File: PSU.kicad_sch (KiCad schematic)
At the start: 55 parts, among them J1 ~12VAC_A, J10 GND, J11 -12V, J12 +5V, J2 ~12VAC_A, J3 ~12VAC_B, J4 ~12VAC_B, J9 +12V, U1 LM317_TO-220, U2 LM317_TO-220, U3 LM337_TO220

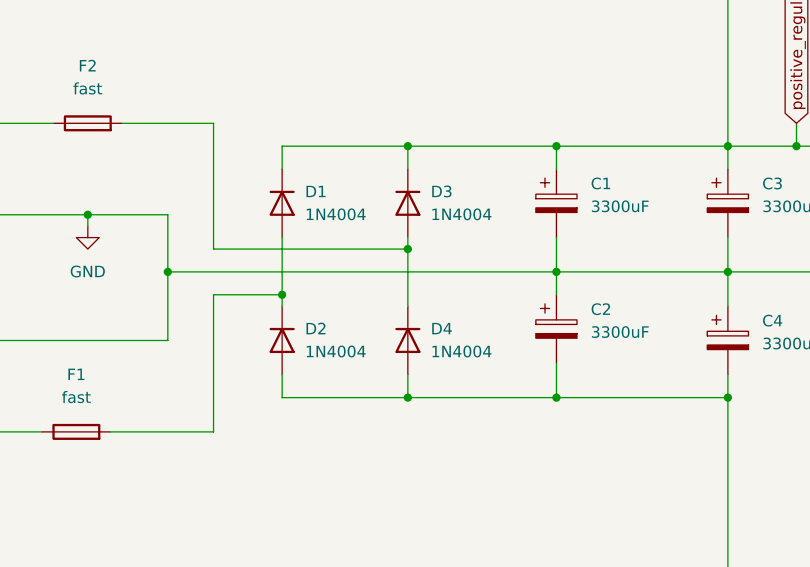
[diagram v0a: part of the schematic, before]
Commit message: Swap rectifier diodes for larger ones. Change input terminal text to be more legible.
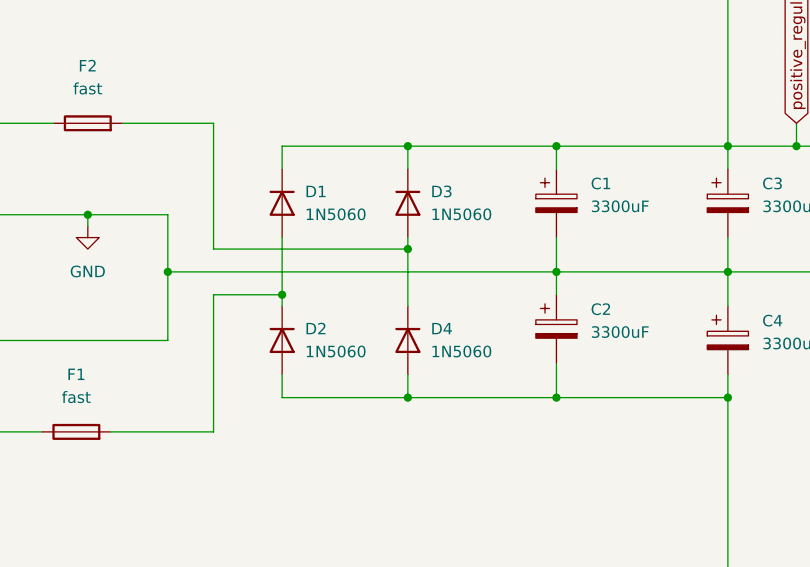
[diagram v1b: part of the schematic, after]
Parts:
- D1, D2, D3, D4: value 1N4004 -> 1N5060
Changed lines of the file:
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@@
       (effects (font (size 1.27 1.27)) (justify left))
     )
-    (property "Value" "1N4004" (id 1) (at 87.63 104.1399 90)
+    (property "Value" "1N5060" (id 1) (at 87.63 104.1399 90)
       (effects (font (size 1.27 1.27)) (justify left))
     )
@@
       (effects (font (size 1.27 1.27)) (justify left))
     )
-    (property "Value" "1N4004" (id 1) (at 101.6 104.1399 90)
+    (property "Value" "1N5060" (id 1) (at 101.6 104.1399 90)
       (effects (font (size 1.27 1.27)) (justify left))
     )
@@
       (effects (font (size 1.27 1.27)) (justify left))
     )
-    (property "Value" "1N4004" (id 1) (at 101.6 88.8999 90)
+    (property "Value" "1N5060" (id 1) (at 101.6 88.8999 90)
       (effects (font (size 1.27 1.27)) (justify left))
     )
@@
       (effects (font (size 1.27 1.27)) (justify left))
     )
-    (property "Value" "1N4004" (id 1) (at 87.63 88.8999 90)
+    (property "Value" "1N5060" (id 1) (at 87.63 88.8999 90)
       (effects (font (size 1.27 1.27)) (justify left))
     )
@@
     )
     (path "/f34b4507-f5d7-4b15-9ede-8d76d9cea360"
-      (reference "D1") (unit 1) (value "1N4004") (footprint "Diode_THT:D_DO-41_SOD81_P10.16mm_Horizontal")
+      (reference "D1") (unit 1) (value "1N5060") (footprint "Diode_THT:D_DO-41_SOD81_P10.16mm_Horizontal")
     )
     (path "/31c7e7d4-2566-4ceb-b304-6dfc36679056"
-      (reference "D2") (unit 1) (value "1N4004") (footprint "Diode_THT:D_DO-41_SOD81_P10.16mm_Horizontal")
+      (reference "D2") (unit 1) (value "1N5060") (footprint "Diode_THT:D_DO-41_SOD81_P10.16mm_Horizontal")
     )
     (path "/9705ebf1-c2ec-44a4-8cff-df85e62870ac"
-      (reference "D3") (unit 1) (value "1N4004") (footprint "Diode_THT:D_DO-41_SOD81_P10.16mm_Horizontal")
+      (reference "D3") (unit 1) (value "1N5060") (footprint "Diode_THT:D_DO-41_SOD81_P10.16mm_Horizontal")
     )
     (path "/5937859a-61e8-45ba-9ebc-1202e95598fd"
-      (reference "D4") (unit 1) (value "1N4004") (footprint "Diode_THT:D_DO-41_SOD81_P10.16mm_Horizontal")
+      (reference "D4") (unit 1) (value "1N5060") (footprint "Diode_THT:D_DO-41_SOD81_P10.16mm_Horizontal")
     )
     (path "/c155e713-676d-49b4-a2d9-40174c28c34c"

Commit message: Edit input label text
Change input labels for improved legibility
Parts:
- D1, D2, D3, D4: footprint Diode_THT:D_DO-41_SOD81_P10.16mm_Horizontal -> Diode_THT:D_DO-15_P10.16mm_Horizontal
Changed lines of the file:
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@@
   (title_block
     (title "Eurorack PSU")
-    (rev "0.1.0")
+    (rev "0.2.0")
     (company "Butch Warns")
   )
@@
       (effects (font (size 1.27 1.27)) (justify left))
     )
-    (property "Footprint" "Diode_THT:D_DO-41_SOD81_P10.16mm_Horizontal" (id 2) (at 80.645 102.87 0)
+    (property "Footprint" "Diode_THT:D_DO-15_P10.16mm_Horizontal" (id 2) (at 80.645 102.87 0)
       (effects (font (size 1.27 1.27)) hide)
     )
@@
       (effects (font (size 1.27 1.27)) (justify left))
     )
-    (property "Footprint" "Diode_THT:D_DO-41_SOD81_P10.16mm_Horizontal" (id 2) (at 94.615 102.87 0)
+    (property "Footprint" "Diode_THT:D_DO-15_P10.16mm_Horizontal" (id 2) (at 94.615 102.87 0)
       (effects (font (size 1.27 1.27)) hide)
     )
@@
       (effects (font (size 1.27 1.27)) (justify left))
     )
-    (property "Footprint" "Diode_THT:D_DO-41_SOD81_P10.16mm_Horizontal" (id 2) (at 94.615 87.63 0)
+    (property "Footprint" "Diode_THT:D_DO-15_P10.16mm_Horizontal" (id 2) (at 94.615 87.63 0)
       (effects (font (size 1.27 1.27)) hide)
     )
@@
       (effects (font (size 1.27 1.27)) (justify left))
     )
-    (property "Footprint" "Diode_THT:D_DO-41_SOD81_P10.16mm_Horizontal" (id 2) (at 80.645 87.63 0)
+    (property "Footprint" "Diode_THT:D_DO-15_P10.16mm_Horizontal" (id 2) (at 80.645 87.63 0)
       (effects (font (size 1.27 1.27)) hide)
     )
@@
     )
     (path "/f34b4507-f5d7-4b15-9ede-8d76d9cea360"
-      (reference "D1") (unit 1) (value "1N5060") (footprint "Diode_THT:D_DO-41_SOD81_P10.16mm_Horizontal")
+      (reference "D1") (unit 1) (value "1N5060") (footprint "Diode_THT:D_DO-15_P10.16mm_Horizontal")
     )
     (path "/31c7e7d4-2566-4ceb-b304-6dfc36679056"
-      (reference "D2") (unit 1) (value "1N5060") (footprint "Diode_THT:D_DO-41_SOD81_P10.16mm_Horizontal")
+      (reference "D2") (unit 1) (value "1N5060") (footprint "Diode_THT:D_DO-15_P10.16mm_Horizontal")
     )
     (path "/9705ebf1-c2ec-44a4-8cff-df85e62870ac"
-      (reference "D3") (unit 1) (value "1N5060") (footprint "Diode_THT:D_DO-41_SOD81_P10.16mm_Horizontal")
+      (reference "D3") (unit 1) (value "1N5060") (footprint "Diode_THT:D_DO-15_P10.16mm_Horizontal")
     )
     (path "/5937859a-61e8-45ba-9ebc-1202e95598fd"
-      (reference "D4") (unit 1) (value "1N5060") (footprint "Diode_THT:D_DO-41_SOD81_P10.16mm_Horizontal")
+      (reference "D4") (unit 1) (value "1N5060") (footprint "Diode_THT:D_DO-15_P10.16mm_Horizontal")
     )
     (path "/c155e713-676d-49b4-a2d9-40174c28c34c"

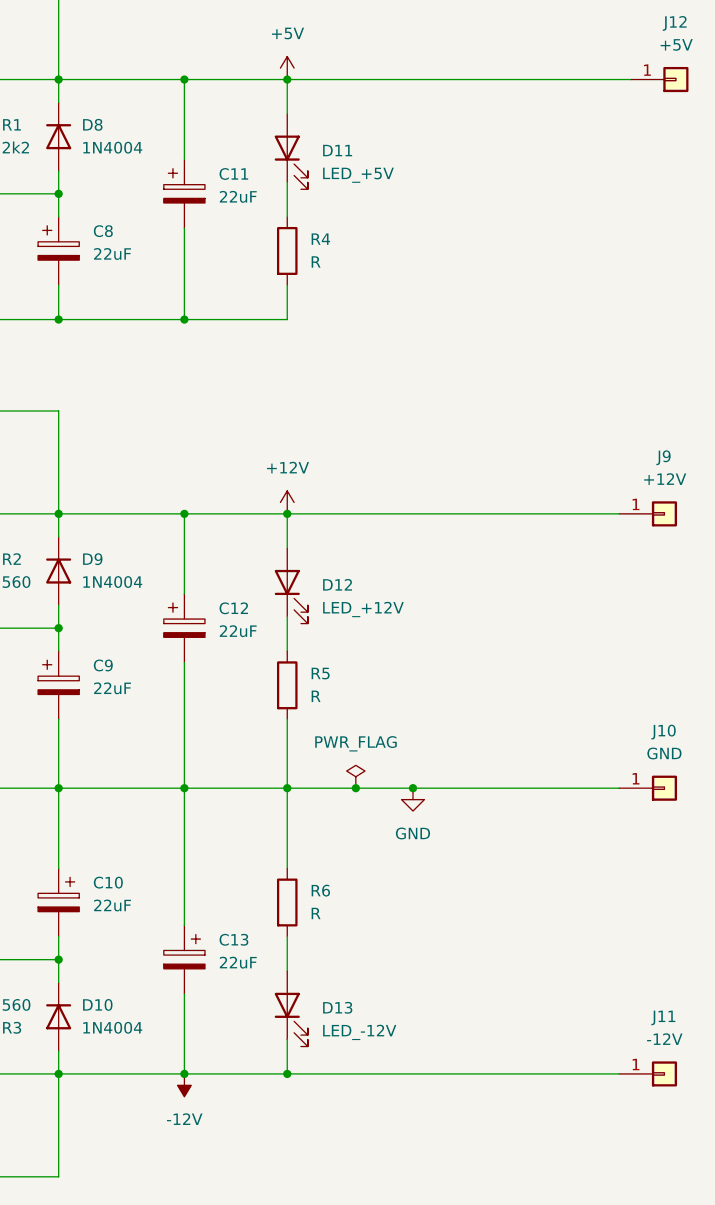
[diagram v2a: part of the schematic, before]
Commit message: Do some small touches before making repo public
Add v010 Gerber files. Add interactive HTML BOM. Set values for LED
current limiting resistors.
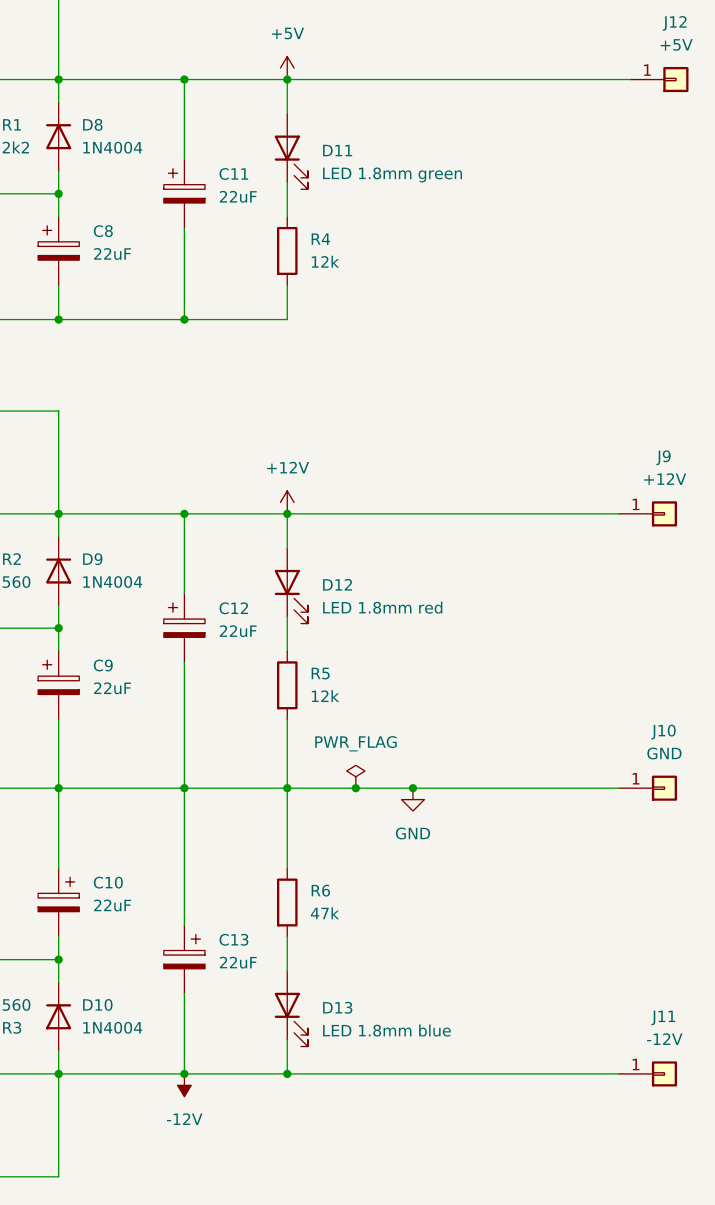
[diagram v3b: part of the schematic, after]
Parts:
- D11: value LED_+5V -> LED 1.8mm green
- D12: value LED_+12V -> LED 1.8mm red
- D13: value LED_-12V -> LED 1.8mm blue
- R4, R5: value R -> 12k
- R6: value R -> 47k
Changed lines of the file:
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@@
       (effects (font (size 1.27 1.27)) (justify right))
     )
-    (property "Value" "LED_-12V" (id 1) (at 222.25 138.7474 90)
+    (property "Value" "LED 1.8mm blue" (id 1) (at 222.25 138.7474 90)
       (effects (font (size 1.27 1.27)) (justify right))
     )
@@
       (effects (font (size 1.27 1.27)) (justify right))
     )
-    (property "Value" "LED_+5V" (id 1) (at 222.25 43.4974 90)
+    (property "Value" "LED 1.8mm green" (id 1) (at 222.25 43.4974 90)
       (effects (font (size 1.27 1.27)) (justify right))
     )
@@
       (effects (font (size 1.27 1.27)) (justify left))
     )
-    (property "Value" "R" (id 1) (at 220.98 101.5999 0)
+    (property "Value" "12k" (id 1) (at 220.98 101.5999 0)
       (effects (font (size 1.27 1.27)) (justify left))
     )
@@
       (effects (font (size 1.27 1.27)) (justify right))
     )
-    (property "Value" "LED_+12V" (id 1) (at 222.25 91.7574 90)
+    (property "Value" "LED 1.8mm red" (id 1) (at 222.25 91.7574 90)
       (effects (font (size 1.27 1.27)) (justify right))
     )
@@
       (effects (font (size 1.27 1.27)) (justify left))
     )
-    (property "Value" "R" (id 1) (at 220.98 53.3399 0)
+    (property "Value" "12k" (id 1) (at 220.98 53.3399 0)
       (effects (font (size 1.27 1.27)) (justify left))
     )
@@
       (effects (font (size 1.27 1.27)) (justify left))
     )
-    (property "Value" "R" (id 1) (at 220.98 125.7299 0)
+    (property "Value" "47k" (id 1) (at 220.98 125.7299 0)
       (effects (font (size 1.27 1.27)) (justify left))
     )
@@
     )
     (path "/1a920980-a2b1-45eb-ac3e-2649db811b22"
-      (reference "D11") (unit 1) (value "LED_+5V") (footprint "LED_THT:LED_D3.0mm")
+      (reference "D11") (unit 1) (value "LED 1.8mm green") (footprint "LED_THT:LED_D3.0mm")
     )
     (path "/7a29d124-ffbb-483f-8475-3c260e713647"
-      (reference "D12") (unit 1) (value "LED_+12V") (footprint "LED_THT:LED_D3.0mm")
+      (reference "D12") (unit 1) (value "LED 1.8mm red") (footprint "LED_THT:LED_D3.0mm")
     )
     (path "/05521341-4993-41a8-8e86-233c58d1545c"
-      (reference "D13") (unit 1) (value "LED_-12V") (footprint "LED_THT:LED_D3.0mm")
+      (reference "D13") (unit 1) (value "LED 1.8mm blue") (footprint "LED_THT:LED_D3.0mm")
     )
     (path "/e7f7fe4f-ebfb-471a-976d-2ea6e6769e03"
@@
     )
     (path "/8bf15c7b-f15f-4a8b-a9a2-ac115433038f"
-      (reference "R4") (unit 1) (value "R") (footprint "Resistor_THT:R_Axial_DIN0207_L6.3mm_D2.5mm_P7.62mm_Horizontal")
+      (reference "R4") (unit 1) (value "12k") (footprint "Resistor_THT:R_Axial_DIN0207_L6.3mm_D2.5mm_P7.62mm_Horizontal")
     )
     (path "/4d8cb080-1bed-4fdd-a077-e915dc4fb9eb"
-      (reference "R5") (unit 1) (value "R") (footprint "Resistor_THT:R_Axial_DIN0207_L6.3mm_D2.5mm_P7.62mm_Horizontal")
+      (reference "R5") (unit 1) (value "12k") (footprint "Resistor_THT:R_Axial_DIN0207_L6.3mm_D2.5mm_P7.62mm_Horizontal")
     )
     (path "/eae44fa8-75b9-45b0-b4a0-25dcf086bf08"
-      (reference "R6") (unit 1) (value "R") (footprint "Resistor_THT:R_Axial_DIN0207_L6.3mm_D2.5mm_P7.62mm_Horizontal")
+      (reference "R6") (unit 1) (value "47k") (footprint "Resistor_THT:R_Axial_DIN0207_L6.3mm_D2.5mm_P7.62mm_Horizontal")
     )
     (path "/e2806f52-7983-4019-b82b-2fa01a314ee9"
